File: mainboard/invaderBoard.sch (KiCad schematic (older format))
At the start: 4 parts

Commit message: kicad version 5 update
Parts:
- P?: symbol CONN_01X02 -> invaderBoard-rescue:CONN_01X02
- P?: symbol CONN_01X03 -> invaderBoard-rescue:CONN_01X03
- Q? (x2): symbol IRF540N -> invaderBoard-rescue:IRF540N
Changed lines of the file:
@@
-EESchema Schematic File Version 2
-LIBS:power
-LIBS:device
-LIBS:transistors
-LIBS:conn
-LIBS:linear
-LIBS:regul
-LIBS:74xx
-LIBS:cmos4000
-LIBS:adc-dac
-LIBS:memory
-LIBS:xilinx
-LIBS:microcontrollers
-LIBS:dsp
-LIBS:microchip
-LIBS:analog_switches
-LIBS:motorola
-LIBS:texas
-LIBS:intel
-LIBS:audio
-LIBS:interface
-LIBS:digital-audio
-LIBS:philips
-LIBS:display
-LIBS:cypress
-LIBS:siliconi
-LIBS:opto
-LIBS:atmel
-LIBS:contrib
-LIBS:valves
-EELAYER 25 0
+EESchema Schematic File Version 4
+LIBS:invaderBoard-cache
+EELAYER 29 0
 EELAYER END
 $Descr A4 11693 8268
@@
 $EndDescr
 $Comp
-L CONN_01X02 P?
+L invaderBoard-rescue:CONN_01X02 P?
 U 1 1 5CC6A607
 P 2300 2125
@@
 $EndComp
 $Comp
-L CONN_01X03 P?
+L invaderBoard-rescue:CONN_01X03 P?
 U 1 1 5CC6A69C
 P 2275 2875
@@
 $EndComp
 $Comp
-L IRF540N Q?
+L invaderBoard-rescue:IRF540N Q?
 U 1 1 5CC6A70B
 P 4700 2200
@@
 $EndComp
 $Comp
-L IRF540N Q?
+L invaderBoard-rescue:IRF540N Q?
 U 1 1 5CC6A75C
 P 5900 2200

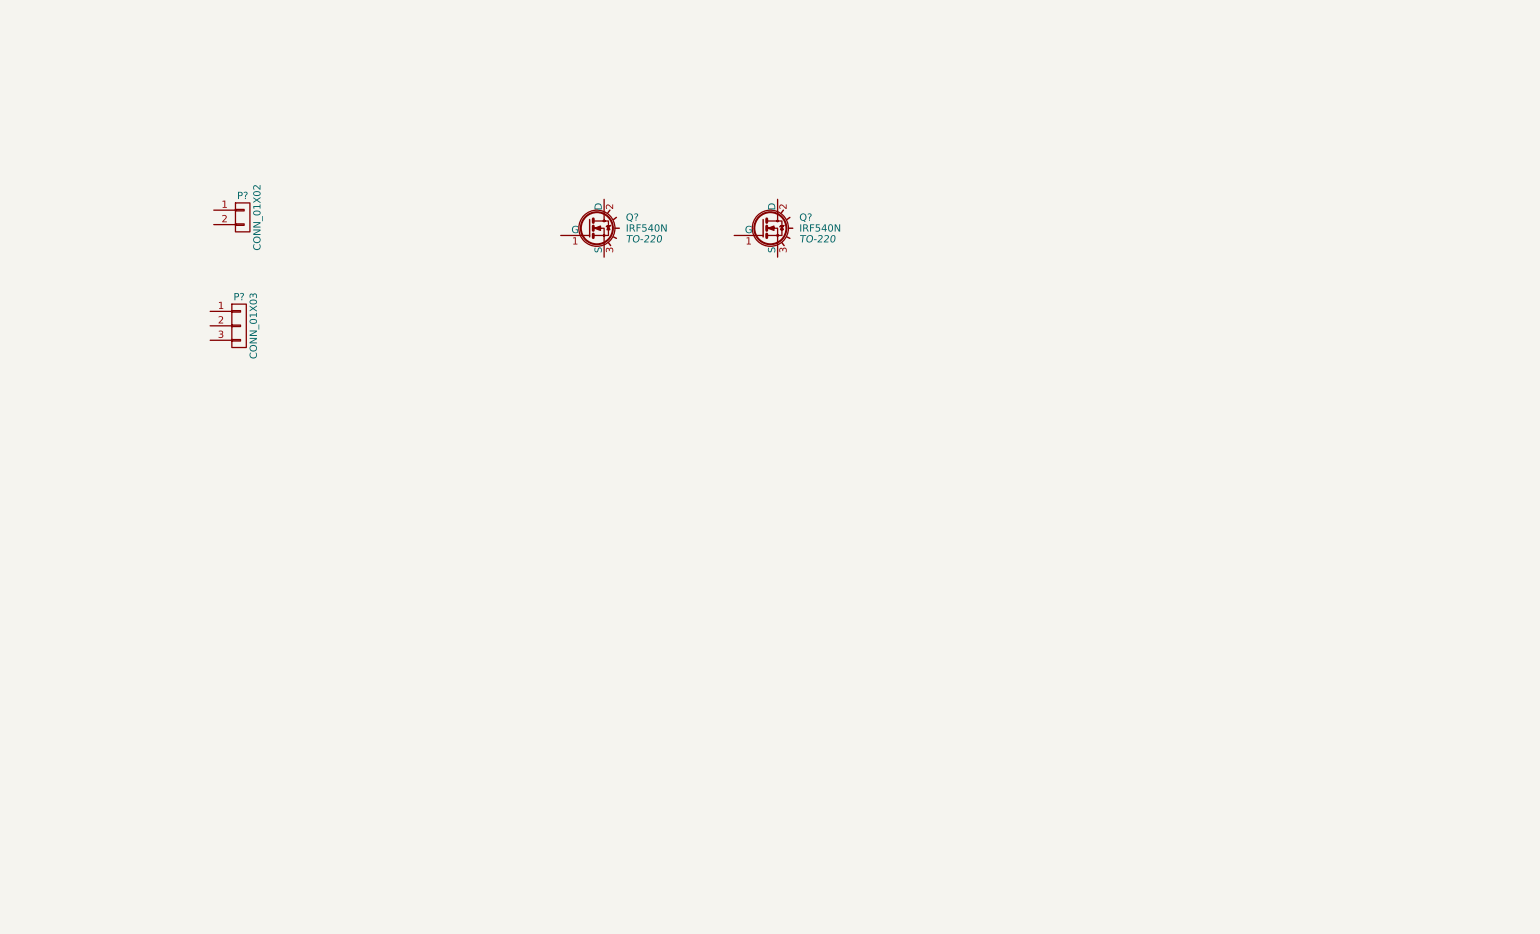
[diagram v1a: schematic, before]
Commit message: Mainboard schematics mostly done
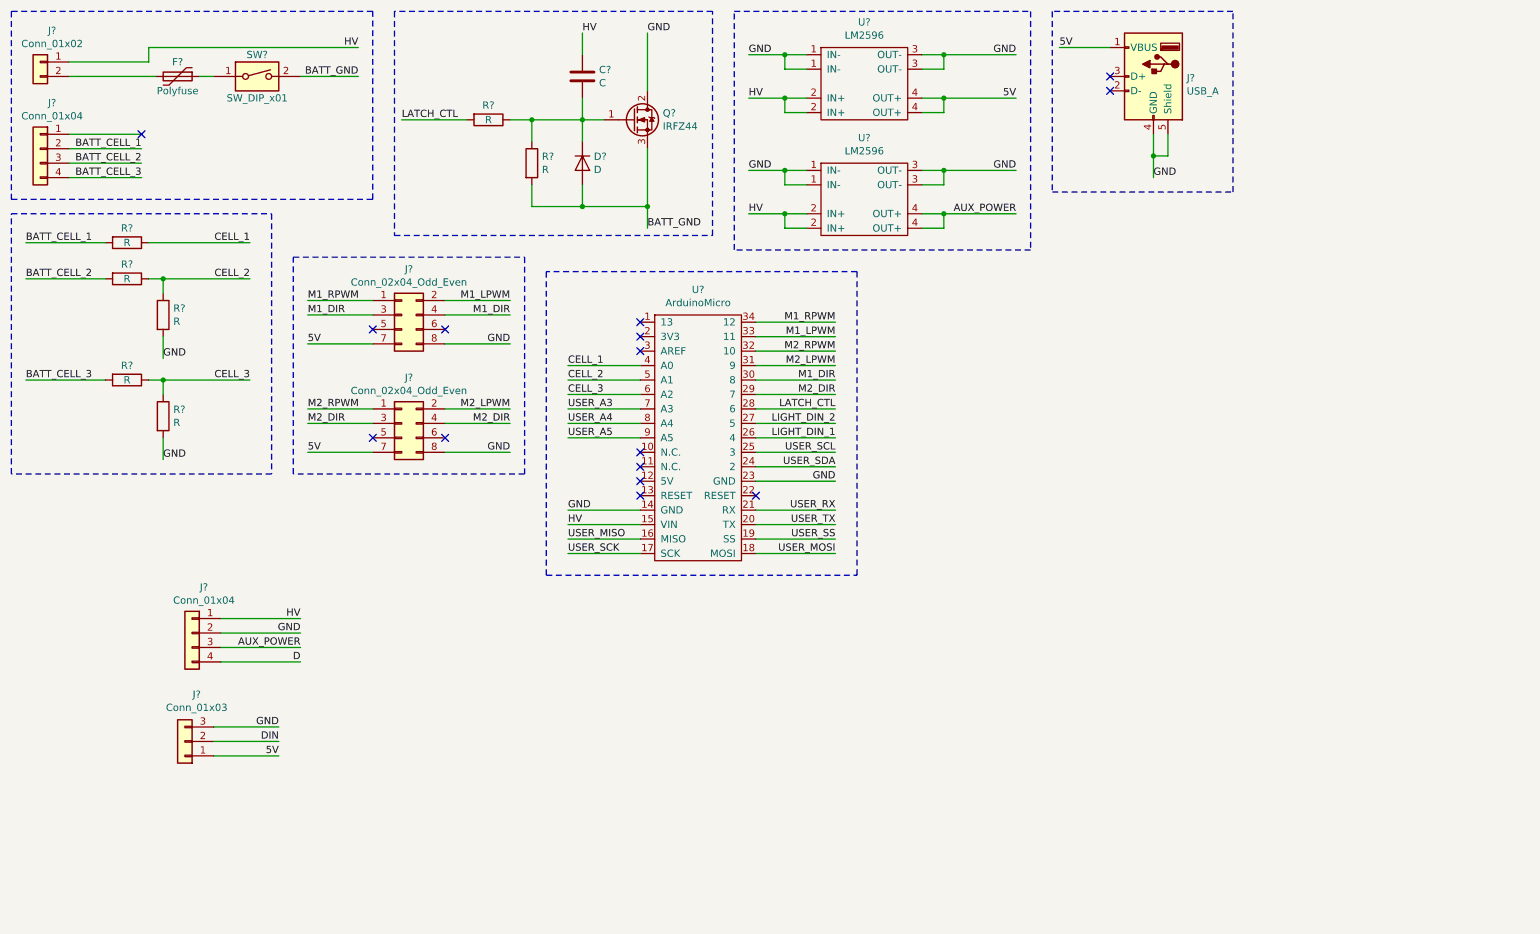
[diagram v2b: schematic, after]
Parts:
- removed P?: CONN_01X02, symbol invaderBoard-rescue:CONN_01X02
- removed P?: CONN_01X03, symbol invaderBoard-rescue:CONN_01X03
- removed Q? (x2): IRF540N, TO-220, symbol invaderBoard-rescue:IRF540N
- added C?: C, symbol Device:C
- added D?: D, symbol Device:D
- added F?: Polyfuse, symbol Device:Polyfuse
- added J?: Conn_01x02, symbol Connector_Generic:Conn_01x02
- added J? (x2): Conn_01x04, symbol Connector_Generic:Conn_01x04
- added J?: USB_A, symbol Connector:USB_A
- added J? (x2): Conn_02x04_Odd_Even, symbol Connector_Generic:Conn_02x04_Odd_Even
- added J?: Conn_01x03, symbol Connector_Generic:Conn_01x03
- added Q?: IRFZ44, Package_TO_SOT_THT:TO-220-3_Vertical, symbol Transistor_FET:IRF540N
- added R? (x7): R, symbol Device:R
- added SW?: SW_DIP_x01, symbol Switch:SW_DIP_x01
- added U? (x2): LM2596, symbol bluerSaab:LM2596
- added U?: ArduinoMicro, symbol invaderBot:ArduinoMicro
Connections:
- new net: F?.2, J?.2 (Pin_2)
- new net: F?.1, SW?.1
- new net: C?.2, D?.1 (K), Q?.1 (G), R?.1, R?.1
- new net 5V: J?.1 (Pin_1), J?.1 (VBUS), J?.7 (Pin_7), J?.7 (Pin_7), U?.4 (OUT+)
- new net AUX_POWER: J?.3 (Pin_3), U?.4 (OUT+)
- new net BATT_CELL_1: J?.2 (Pin_2), R?.2
- new net BATT_CELL_2: J?.3 (Pin_3), R?.2
- new net BATT_CELL_3: J?.4 (Pin_4), R?.2
- new net BATT_GND: D?.2 (A), Q?.3 (S), R?.2, SW?.2
- new net CELL_1: R?.1, U?.4 (A0)
- new net CELL_2: R?.1, R?.1, U?.5 (A1)
- new net CELL_3: R?.1, R?.1, U?.6 (A2)
- new net D: J?.4 (Pin_4)
- new net DIN: J?.2 (Pin_2)
- new net GND: J?.2 (Pin_2), J?.3 (Pin_3), J?.4 (GND), J?.5 (Shield), J?.8 (Pin_8), J?.8 (Pin_8), Q?.2 (D), R?.2, R?.2, U?.1 (IN-), U?.1 (IN-), U?.14 (GND), U?.23 (GND), U?.3 (OUT-), U?.3 (OUT-)
- new net HV: C?.1, J?.1 (Pin_1), J?.1 (Pin_1), U?.15 (VIN), U?.2 (IN+), U?.2 (IN+)
- new net LATCH_CTL: R?.2, U?.28 (6)
- new net LIGHT_DIN_1: U?.26 (4)
- new net LIGHT_DIN_2: U?.27 (5)
- new net M1_DIR: J?.3 (Pin_3), J?.4 (Pin_4), U?.30 (8)
- new net M1_LPWM: J?.2 (Pin_2), U?.33 (11)
- new net M1_RPWM: J?.1 (Pin_1), U?.34 (12)
- new net M2_DIR: J?.3 (Pin_3), J?.4 (Pin_4), U?.29 (7)
- new net M2_LPWM: J?.2 (Pin_2), U?.31 (9)
- new net M2_RPWM: J?.1 (Pin_1), U?.32 (10)
- new net USER_A3: U?.7 (A3)
- new net USER_A4: U?.8 (A4)
- new net USER_A5: U?.9 (A5)
- new net USER_MISO: U?.16 (MISO)
- new net USER_MOSI: U?.18 (MOSI)
- new net USER_RX: U?.21 (RX)
- new net USER_SCK: U?.17 (SCK)
- new net USER_SCL: U?.25 (3)
- new net USER_SDA: U?.24 (2)
- new net USER_SS: U?.19 (SS)
- new net USER_TX: U?.20 (TX)
- no-connect marks 0 -> 15

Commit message: PCB mostly done, motor power outputs added to schematics
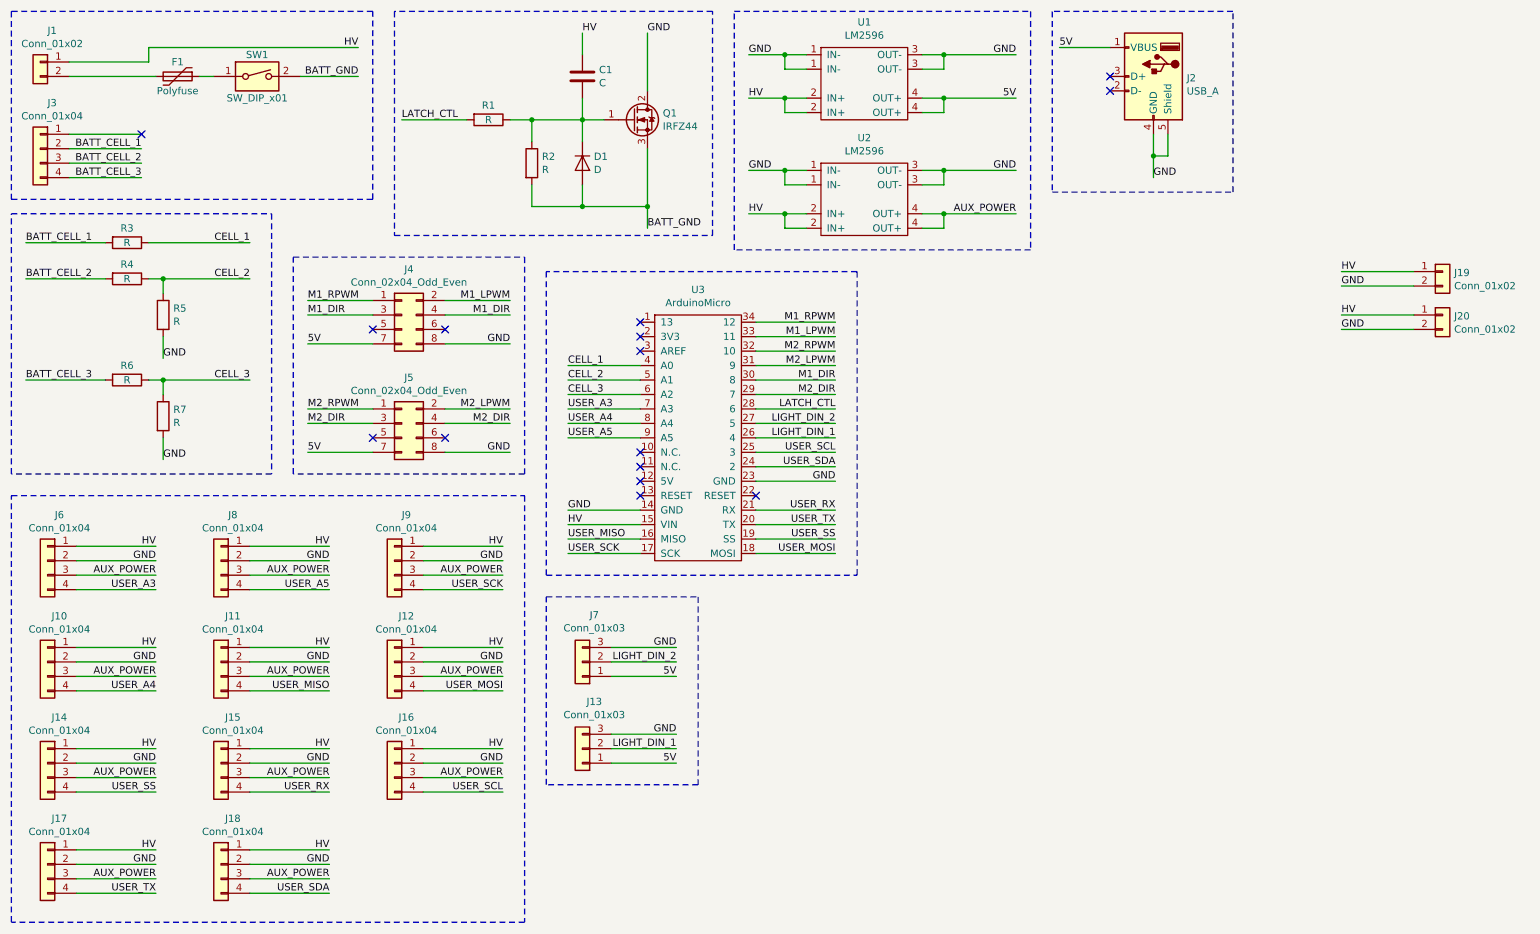
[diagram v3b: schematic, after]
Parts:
- added J10, J11, J12, J14, J15, J16, J17, J18, J8, J9: Conn_01x04, Connector_JST:JST_XH_B4B-XH-A_1x04_P2.50mm_Vertical, symbol Connector_Generic:Conn_01x04
- added J13: Conn_01x03, Connector_JST:JST_XH_S3B-XH-A_1x03_P2.50mm_Horizontal, symbol Connector_Generic:Conn_01x03
- added J19, J20: Conn_01x02, Connector_Wire:SolderWirePad_1x02_P3.81mm_Drill1mm, symbol Connector_Generic:Conn_01x02
- C1: renamed from C?; footprint (none) -> Capacitor_THT:CP_Radial_D8.0mm_P2.50mm
- D1: renamed from D?; footprint (none) -> Diode_THT:D_DO-35_SOD27_P7.62mm_Horizontal
- F1: renamed from F?; footprint (none) -> invaderBoard:PTC Fuse
- J1: renamed from J?; footprint (none) -> Connector_Wire:SolderWirePad_1x02_P7.62mm_Drill2mm
- J2: renamed from J?; footprint (none) -> invaderBoard:USB_A
- J3: renamed from J?; footprint (none) -> Connector_JST:JST_XH_S4B-XH-A_1x04_P2.50mm_Horizontal
- J4, J5: renamed from J?; footprint (none) -> Connector_PinHeader_2.54mm:PinHeader_2x04_P2.54mm_Vertical
- J6: renamed from J?; footprint (none) -> Connector_JST:JST_XH_B4B-XH-A_1x04_P2.50mm_Vertical
- J7: renamed from J?; footprint (none) -> Connector_JST:JST_XH_S3B-XH-A_1x03_P2.50mm_Horizontal
- R1, R2, R3, R4, R5, R6, R7: renamed from R?; footprint (none) -> Resistor_THT:R_Axial_DIN0204_L3.6mm_D1.6mm_P5.08mm_Horizontal
- SW1: renamed from SW?; footprint (none) -> Connector_Wire:SolderWirePad_1x02_P3.81mm_Drill1mm
- U1, U2: renamed from U?; footprint (none) -> bluerSaab:LM2596
- U3: renamed from U?; footprint (none) -> invaderBoard:Arduino Micro
- gave numbers to parts that had none: 1
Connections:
- net D is gone; now on net USER_A3: J6.4 (Pin_4)
- net DIN is gone; now on net LIGHT_DIN_2: J7.2 (Pin_2)
- net 5V: now also J13.1 (Pin_1)
- net AUX_POWER: now also J10.3 (Pin_3), J11.3 (Pin_3), J12.3 (Pin_3), J14.3 (Pin_3), J15.3 (Pin_3), J16.3 (Pin_3), J17.3 (Pin_3), J18.3 (Pin_3), J8.3 (Pin_3), J9.3 (Pin_3)
- net GND: now also J10.2 (Pin_2), J11.2 (Pin_2), J12.2 (Pin_2), J13.3 (Pin_3), J14.2 (Pin_2), J15.2 (Pin_2), J16.2 (Pin_2), J17.2 (Pin_2), J18.2 (Pin_2), J19.2 (Pin_2), J20.2 (Pin_2), J8.2 (Pin_2), J9.2 (Pin_2)
- net HV: now also J10.1 (Pin_1), J11.1 (Pin_1), J12.1 (Pin_1), J14.1 (Pin_1), J15.1 (Pin_1), J16.1 (Pin_1), J17.1 (Pin_1), J18.1 (Pin_1), J19.1 (Pin_1), J20.1 (Pin_1), J8.1 (Pin_1), J9.1 (Pin_1)
- net LIGHT_DIN_1: now also J13.2 (Pin_2)
- net USER_A4: now also J10.4 (Pin_4)
- net USER_A5: now also J8.4 (Pin_4)
- net USER_MISO: now also J11.4 (Pin_4)
- net USER_MOSI: now also J12.4 (Pin_4)
- net USER_RX: now also J15.4 (Pin_4)
- net USER_SCK: now also J9.4 (Pin_4)
- net USER_SCL: now also J16.4 (Pin_4)
- net USER_SDA: now also J18.4 (Pin_4)
- net USER_SS: now also J14.4 (Pin_4)
- net USER_TX: now also J17.4 (Pin_4)
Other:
- moved on the sheet: J6, J7

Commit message: Updated PCB - layout done, routing isn't
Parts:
- removed J12, J14, J15, J16, J17, J18, J9: Conn_01x04, Connector_JST:JST_XH_B4B-XH-A_1x04_P2.50mm_Vertical, symbol Connector_Generic:Conn_01x04
- removed U2: LM2596, bluerSaab:LM2596, symbol bluerSaab:LM2596
- J10, J6, J8: value Conn_01x04 -> Conn_01x03; footprint Connector_JST:JST_XH_B4B-XH-A_1x04_P2.50mm_Vertical -> Connector_JST:JST_XH_B3B-XH-A_1x03_P2.50mm_Vertical; symbol Connector_Generic:Conn_01x04 -> Connector_Generic:Conn_01x03
- J13, J7: footprint Connector_JST:JST_XH_S3B-XH-A_1x03_P2.50mm_Horizontal -> Connector_JST:JST_XH_B3B-XH-A_1x03_P2.50mm_Vertical
- R3, R4, R5, R6, R7: footprint Resistor_THT:R_Axial_DIN0204_L3.6mm_D1.6mm_P5.08mm_Horizontal -> Resistor_SMD:R_0805_2012Metric_Pad1.15x1.40mm_HandSolder
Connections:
- net USER_A3: now also J6.3 (Pin_3); no longer J6.4 (Pin_4)
- net USER_A4: now also J10.3 (Pin_3); no longer J10.4 (Pin_4)
- net USER_A5: now also J8.3 (Pin_3); no longer J8.4 (Pin_4)
- net USER_MISO: no longer J11.4 (Pin_4)
- net USER_RX: now also J11.3 (Pin_3)
- net USER_TX: now also J11.4 (Pin_4)
- removed net AUX_POWER: J10.3 (Pin_3), J11.3 (Pin_3), J6.3 (Pin_3), J8.3 (Pin_3)
- no-connect marks 15 -> 21

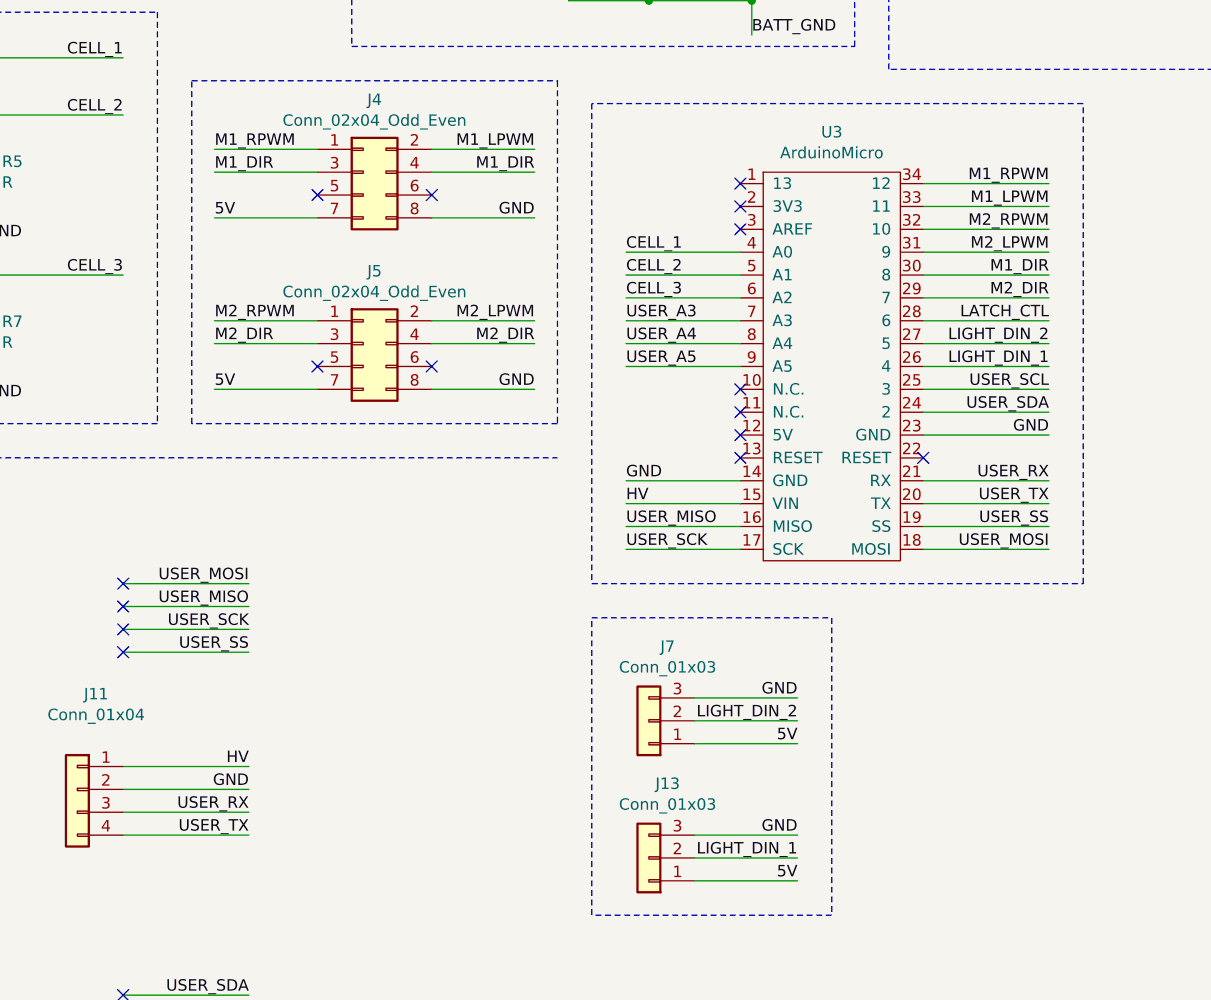
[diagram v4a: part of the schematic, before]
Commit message: PCB Done, some changes on schematics
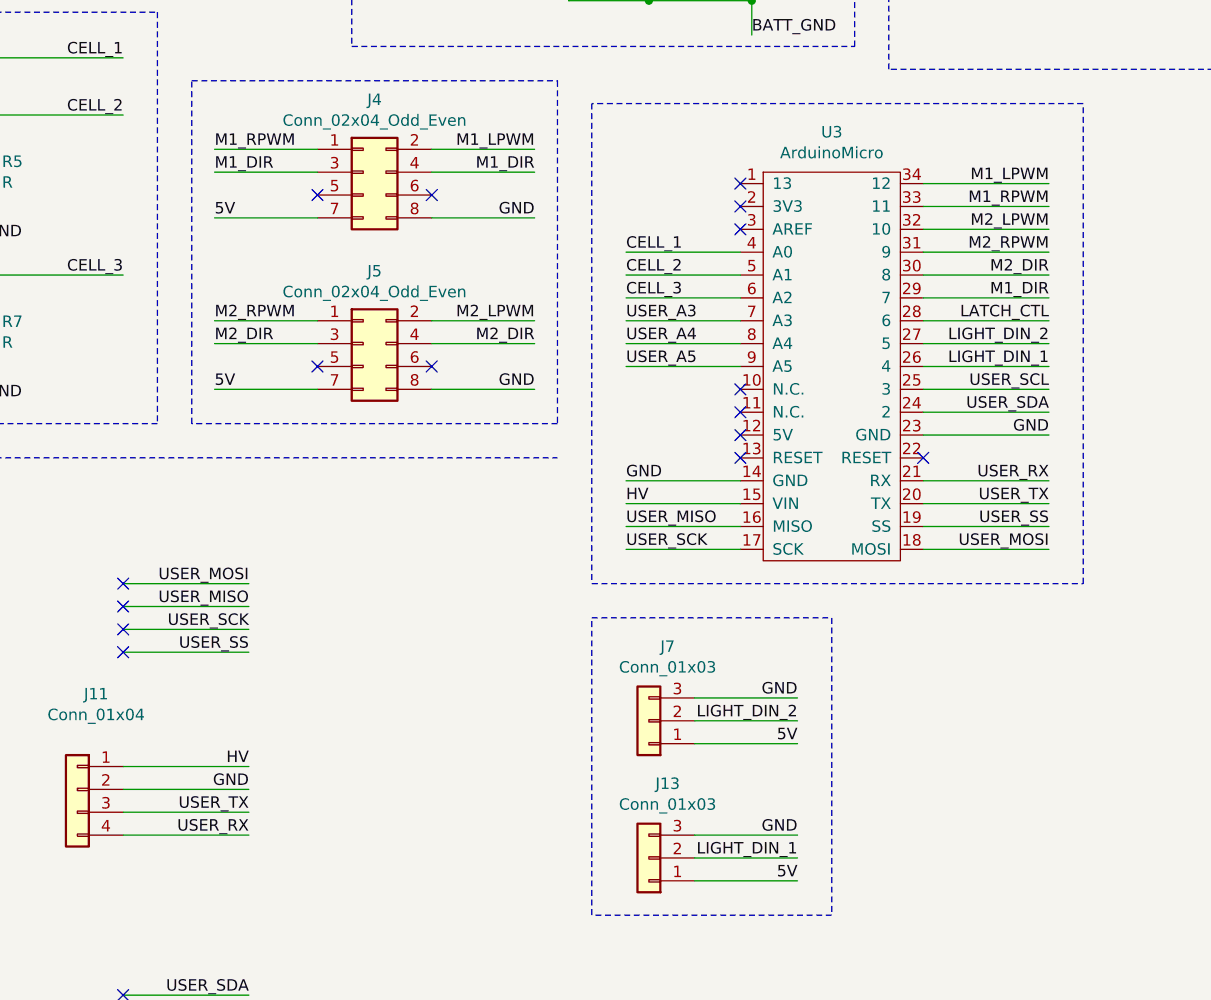
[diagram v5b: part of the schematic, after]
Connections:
- net M1_DIR: now also U3.29 (7); no longer U3.30 (8)
- net M1_LPWM: now also U3.34 (12); no longer U3.33 (11)
- net M1_RPWM: now also U3.33 (11); no longer U3.34 (12)
- net M2_DIR: now also U3.30 (8); no longer U3.29 (7)
- net M2_LPWM: now also U3.32 (10); no longer U3.31 (9)
- net M2_RPWM: now also U3.31 (9); no longer U3.32 (10)
- net USER_RX: now also J11.4 (Pin_4); no longer J11.3 (Pin_3)
- net USER_TX: now also J11.3 (Pin_3); no longer J11.4 (Pin_4)
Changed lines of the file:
@@
 LATCH_CTL
 Text Label 6400 3350 2    50   ~ 0
+M1_DIR
+Text Label 6400 3250 2    50   ~ 0
 M2_DIR
-Text Label 6400 3250 2    50   ~ 0
-M1_DIR
 Text Label 6400 3150 2    50   ~ 0
+M2_RPWM
+Text Label 6400 3050 2    50   ~ 0
 M2_LPWM
-Text Label 6400 3050 2    50   ~ 0
-M2_RPWM
 Text Label 6400 2950 2    50   ~ 0
+M1_RPWM
+Text Label 6400 2850 2    50   ~ 0
 M1_LPWM
-Text Label 6400 2850 2    50   ~ 0
-M1_RPWM
 Wire Wire Line
 	6400 2850 5850 2850
@@
 	2350 6500 2900 6500
 Text Label 2900 5700 2    50   ~ 0
+USER_RX
+Text Label 2900 5600 2    50   ~ 0
 USER_TX
-Text Label 2900 5600 2    50   ~ 0
-USER_RX
 Wire Notes Line
 	700  4050 4250 4050
